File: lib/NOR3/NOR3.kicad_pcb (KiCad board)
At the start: 2 copper layers, 6 parts

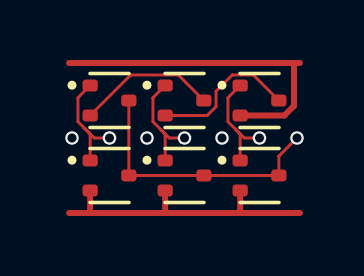
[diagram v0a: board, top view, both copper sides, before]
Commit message: High-density layout with pitch of 1.1mm, which gains 23% !!
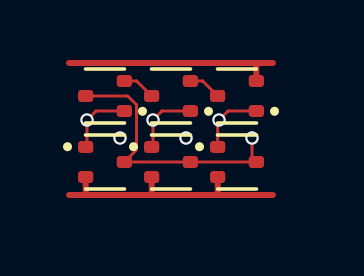
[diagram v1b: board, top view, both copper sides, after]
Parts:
- moved N3 0.87 mm to (5.50, 3.30)
- moved P3 0.76 mm to (5.50, 1.10), turned to 180 degrees
- moved N2 0.64 mm to (3.30, 3.30)
- moved N1 0.47 mm to (1.10, 3.30)
- moved P2 0.47 mm to (3.30, 1.10), turned to 180 degrees
- moved P1 0.21 mm to (1.10, 1.10), turned to 180 degrees
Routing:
- net int2: track 5.00 -> 1.12 mm
- net VDD: track 11.1 -> 7.40 mm
- net int1: track 4.70 -> 1.12 mm
- net C: track 3.87 -> 2.29 mm
- net A: track 3.83 -> 2.29 mm
- net B: track 3.73 -> 2.29 mm
- net GND: track 9.91 -> 8.63 mm
- net (no net): vias 3 -> 2

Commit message: Same for NOR3
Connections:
- net A renamed A1
- net B renamed A2
- net C renamed A3
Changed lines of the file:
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@@
 	(net 1 "GND")
 	(net 2 "Y")
-	(net 3 "C")
+	(net 3 "A3")
 	(net 4 "VDD")
-	(net 5 "A")
-	(net 6 "B")
+	(net 5 "A1")
+	(net 6 "A2")
 	(net 7 "int1")
 	(net 8 "int2")
@@
 			(layers "F.Cu" "F.Mask" "F.Paste")
 			(roundrect_rratio 0.25)
-			(net 6 "B")
+			(net 6 "A2")
 			(pinfunction "G")
 			(pintype "inout")
@@
 			(layers "F.Cu" "F.Mask" "F.Paste")
 			(roundrect_rratio 0.25)
-			(net 3 "C")
+			(net 3 "A3")
 			(pinfunction "G")
 			(pintype "inout")
@@
 			(layers "F.Cu" "F.Mask" "F.Paste")
 			(roundrect_rratio 0.25)
-			(net 3 "C")
+			(net 3 "A3")
 			(pinfunction "G")
 			(pintype "inout")
@@
 			(layers "F.Cu" "F.Mask" "F.Paste")
 			(roundrect_rratio 0.25)
-			(net 5 "A")
+			(net 5 "A1")
 			(pinfunction "G")
 			(pintype "inout")
@@
 			(layers "F.Cu" "F.Mask" "F.Paste")
 			(roundrect_rratio 0.25)
-			(net 5 "A")
+			(net 5 "A1")
 			(pinfunction "G")
 			(pintype "inout")
@@
 			(layers "F.Cu" "F.Mask" "F.Paste")
 			(roundrect_rratio 0.25)
-			(net 6 "B")
+			(net 6 "A2")
 			(pinfunction "G")
 			(pintype "inout")

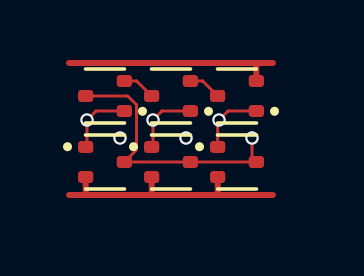
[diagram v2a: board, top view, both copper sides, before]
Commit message: All cells now use 1mm*4mm grid rather than 1.1mm*4.4mm
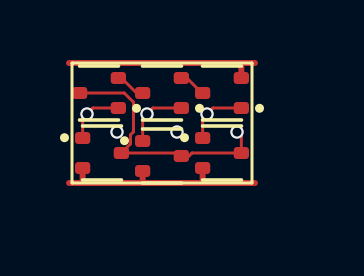
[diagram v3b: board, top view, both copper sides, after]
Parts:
- moved N3 0.58 mm to (5.00, 3.00)
- moved P3 0.51 mm to (5.00, 1.00)
- moved N2 0.36 mm to (3.00, 3.10)
- moved N1 0.32 mm to (1.00, 3.00)
- moved P2 0.32 mm to (3.00, 1.00)
- moved P1 0.22 mm to (0.90, 1.00)
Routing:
- net GND: track 8.63 -> 7.66 mm
- net VDD: track 7.40 -> 6.72 mm
- net Y: track 9.15 -> 8.62 mm

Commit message: Make the pads of my SOT523 footprint very slightly smaller, which is enough to route all the cells and leave the mosfets exactly on the grid
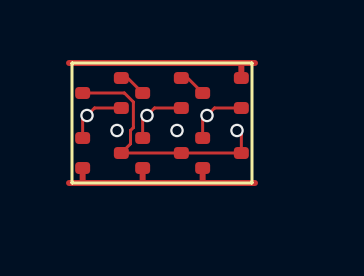
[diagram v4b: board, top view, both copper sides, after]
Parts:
- N1, N2, N3, P1, P2, P3: footprint Package_TO_SOT_SMD:SOT-523 -> RV523:SOT523
- moved N2 0.10 mm to (3.00, 3.00)
- moved P1 0.10 mm to (1.00, 1.00)

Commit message: Propagate MOSFET values to the cells' PCBs
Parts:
- N1, N2, N3: value (none) -> NMOS
- P1, P2, P3: value (none) -> PMOS
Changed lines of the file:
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@@
 			)
 		)
-		(property "Value" ""
+		(property "Value" "PMOS"
 			(at 0 0 180)
 			(layer "F.Fab")
@@
 			)
 		)
-		(property "Value" ""
+		(property "Value" "PMOS"
 			(at 0 0 180)
 			(layer "F.Fab")
@@
 			)
 		)
-		(property "Value" ""
+		(property "Value" "NMOS"
 			(at 0 0 0)
 			(layer "F.Fab")
@@
 			)
 		)
-		(property "Value" ""
+		(property "Value" "PMOS"
 			(at 0 0 180)
 			(layer "F.Fab")
@@
 			)
 		)
-		(property "Value" ""
+		(property "Value" "NMOS"
 			(at 0 0 0)
 			(layer "F.Fab")
@@
 			)
 		)
-		(property "Value" ""
-			(at 0 0 0)
-			(layer "F.Fab")
+		(property "Value" "NMOS"
+			(at 0 0 0)
+			(layer "F.Fab")
